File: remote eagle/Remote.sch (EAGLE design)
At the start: 29 parts, among them U1 ATTINY84-20SSU

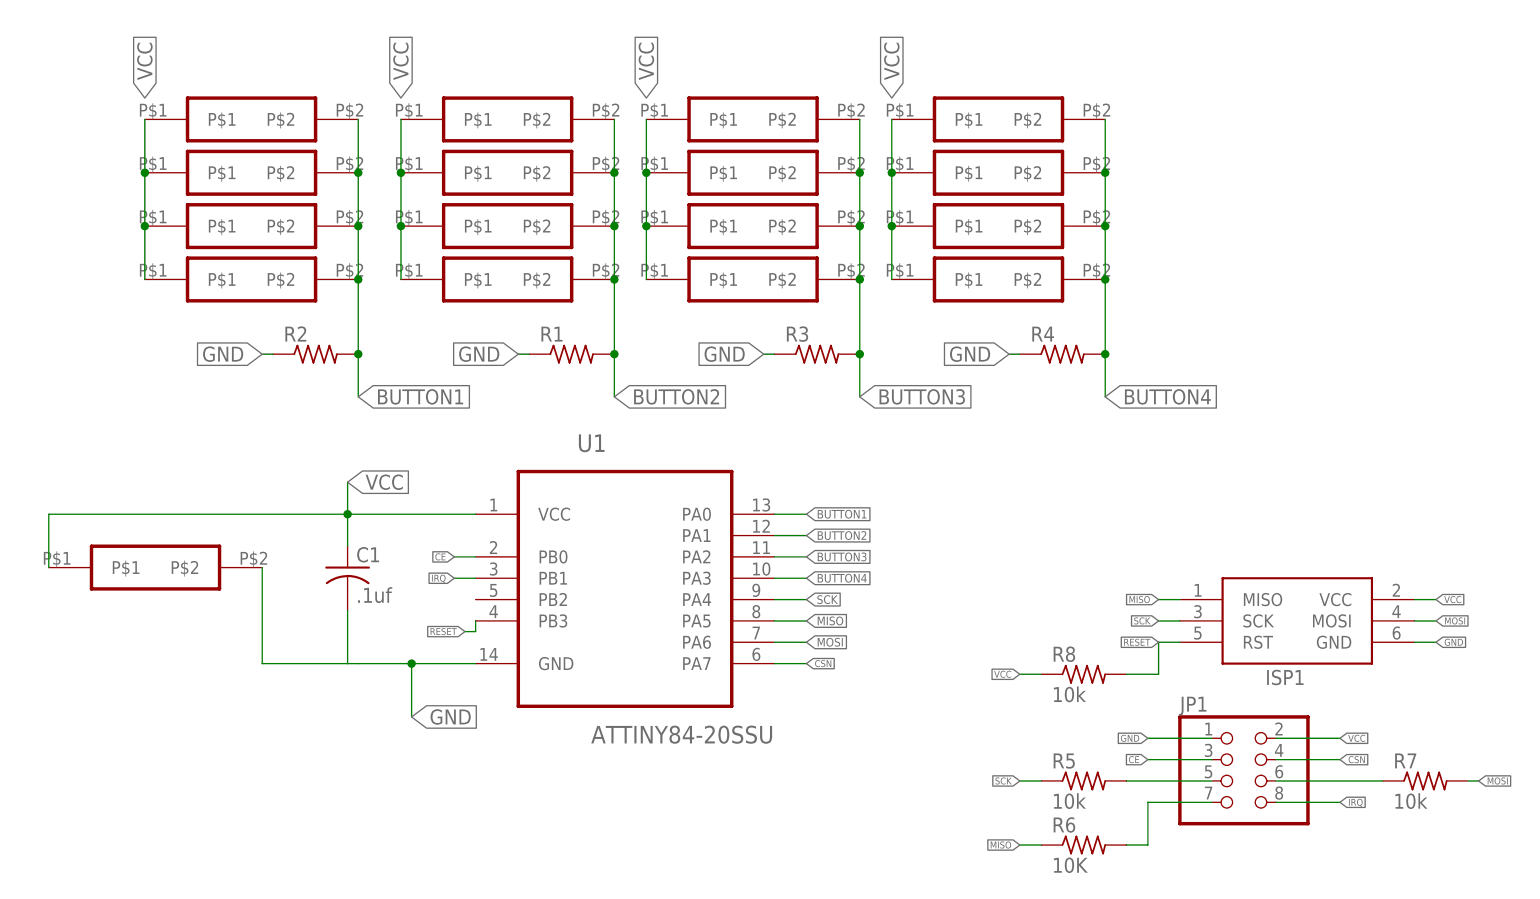
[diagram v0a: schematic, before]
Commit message: Updating remote schematic to include new crystal.
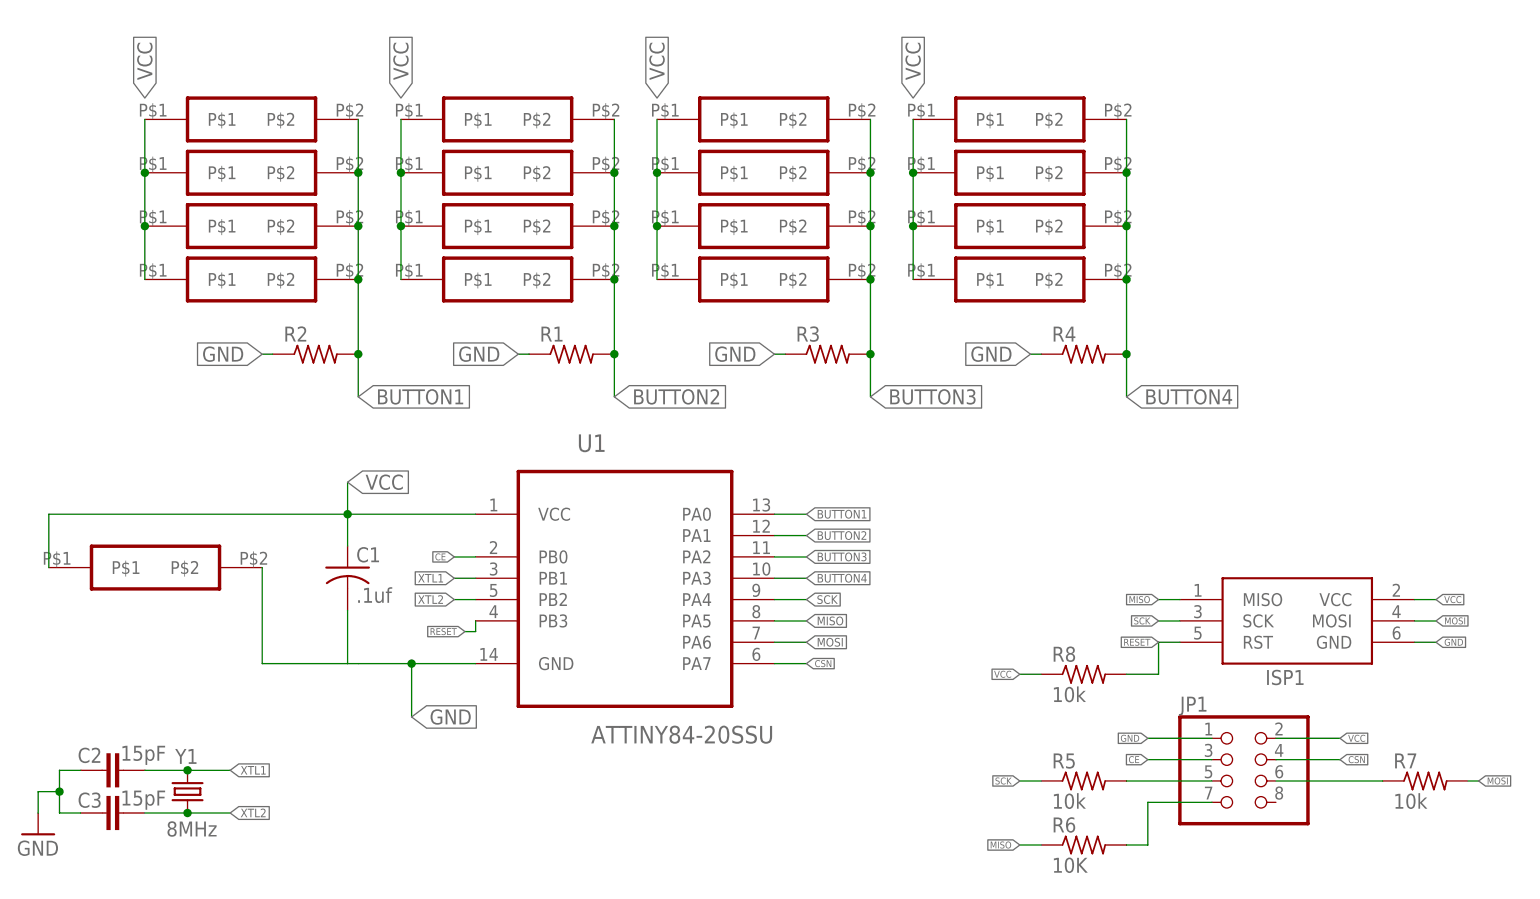
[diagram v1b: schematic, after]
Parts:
- added C2, C3: 15pF, SparkFun:CAP0402-CAP
- added Y1: 8MHz, SparkFun:CRYSTAL5X3
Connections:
- removed net IRQ: JP1.8, U1.PB1
- new net XTL1: C2.2, U1.PB1, Y1.2
- new net XTL2: C3.2, U1.PB2, Y1.1
- net GND: now also C2.1, C3.1
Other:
- moved on the sheet: R3, R4

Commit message: Redrawing remote to fit 1.5" layout. Adding library for new tactile switch with SMD.
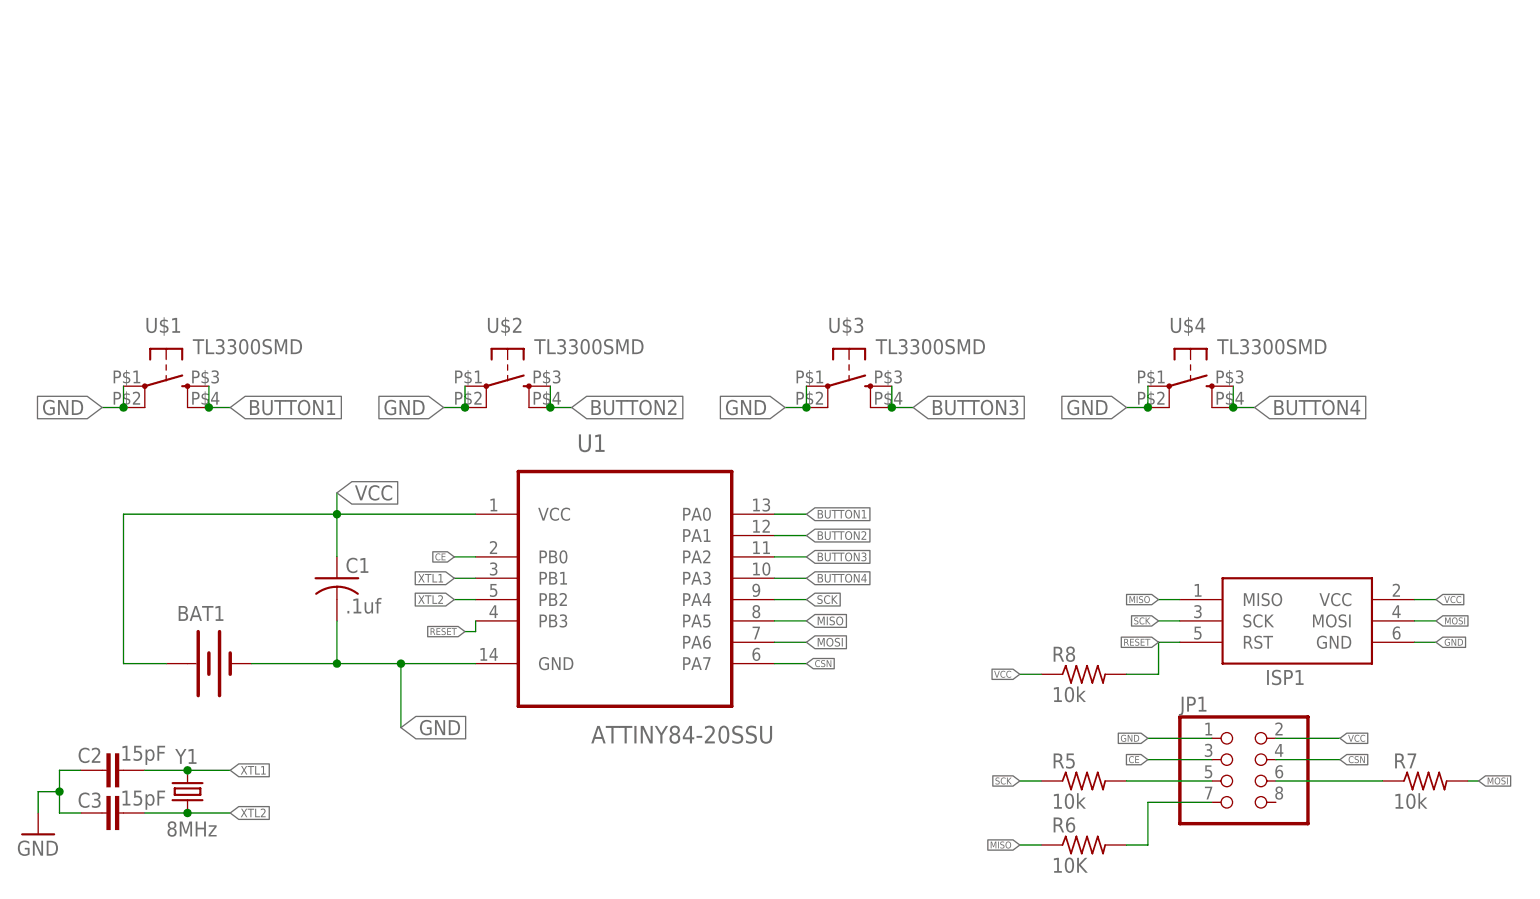
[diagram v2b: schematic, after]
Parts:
- removed BUTTON1-A, BUTTON1-B, BUTTON1-C, BUTTON1-D, BUTTON2-A, BUTTON2-B, BUTTON2-C, BUTTON2-D, BUTTON3-A, BUTTON3-B, BUTTON3-C, BUTTON3-D, BUTTON4-A, BUTTON4-B, BUTTON4-C, BUTTON4-D: BUTTON-25MM-4PAD, solids:BUTTON-25MM-4PAD
- removed R1, R2, R3, R4: (no value), adafruit:R-US_R0805
- added BAT1: (no value), SparkFun-Electromechanical:BATTERY20SMD
- added U$2, U$3, U$4: TL3300SMD, remote:TL3300SMD
- U$1: value A99327CT-ND -> TL3300SMD; device solids:A99327CT-ND -> remote:TL3300SMD
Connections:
- net BUTTON1: now also U$1.S, U$1.S1; no longer BUTTON1-A.P$2, BUTTON1-B.P$2, BUTTON1-C.P$2, BUTTON1-D.P$2, R2.2
- net BUTTON2: now also U$2.S, U$2.S1; no longer BUTTON2-A.P$2, BUTTON2-B.P$2, BUTTON2-C.P$2, BUTTON2-D.P$2, R1.2
- net BUTTON3: now also U$3.S, U$3.S1; no longer BUTTON3-A.P$2, BUTTON3-B.P$2, BUTTON3-C.P$2, BUTTON3-D.P$2, R3.2
- net BUTTON4: now also U$4.S, U$4.S1; no longer BUTTON4-A.P$2, BUTTON4-B.P$2, BUTTON4-C.P$2, BUTTON4-D.P$2, R4.2
- net GND: now also BAT1.-, U$1.P, U$1.P1, U$2.P, U$2.P1, U$3.P, U$3.P1, U$4.P, U$4.P1; no longer R1.1, R2.1, R3.1, R4.1, U$1.P$2
- net VCC: now also BAT1.+; no longer BUTTON1-A.P$1, BUTTON1-B.P$1, BUTTON1-C.P$1, BUTTON1-D.P$1, BUTTON2-A.P$1, BUTTON2-B.P$1, BUTTON2-C.P$1, BUTTON2-D.P$1, BUTTON3-A.P$1, BUTTON3-B.P$1, BUTTON3-C.P$1, BUTTON3-D.P$1, BUTTON4-A.P$1, BUTTON4-B.P$1, BUTTON4-C.P$1, BUTTON4-D.P$1, U$1.P$1
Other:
- moved on the sheet: C1

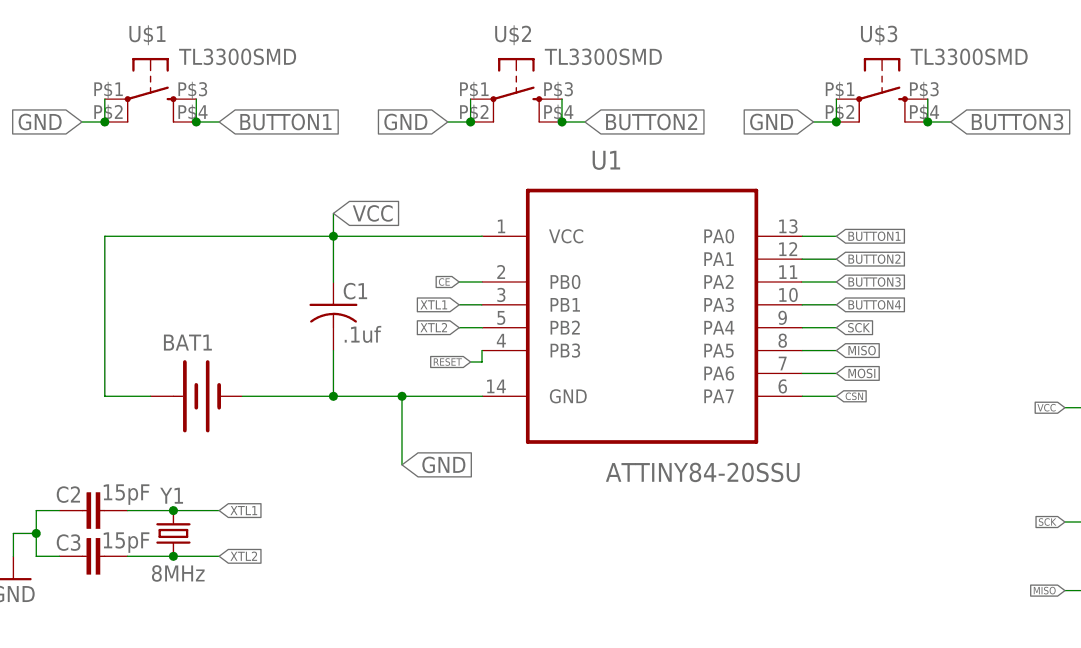
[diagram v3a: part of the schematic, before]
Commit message: Finishing up electrical connections. Replacing battery holder with double-pronged sides.
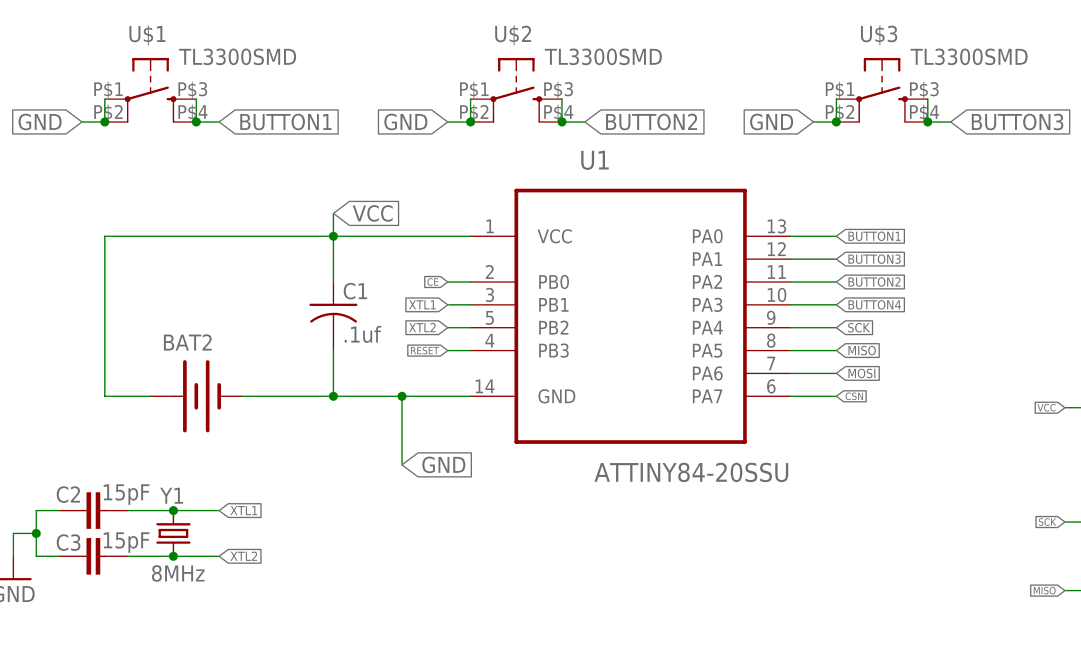
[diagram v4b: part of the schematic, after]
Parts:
- removed BAT1: (no value), SparkFun-Electromechanical:BATTERY20SMD
- added BAT2: (no value), SparkFun-Electromechanical:BATTERY20MM_4LEGS_OVERPASTE
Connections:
- net BUTTON2: now also U1.PA2; no longer U1.PA1
- net BUTTON3: now also U1.PA1; no longer U1.PA2
- net GND: now also BAT2.-; no longer BAT1.-
- net VCC: now also BAT2.+; no longer BAT1.+
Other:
- moved on the sheet: U1

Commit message: Finishing remote rev. 2 board with new buttons and bigger size.
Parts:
- removed C2, C3: 15pF, SparkFun:CAP0402-CAP
- added C5, C6: 15pF, SparkFun-Passives:CAP0805
- U$1, U$2, U$3, U$4: value TL3300SMD -> 5GSH9; device remote:TL3300SMD -> remote:5GSH9
- renumbered ISP1 to ISP, JP1 to NRF24L01, U1 to ATTINY84
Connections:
- net CE: now also ATTINY84.PB2; no longer ATTINY84.PB0
- net GND: now also C5.1, C6.1; no longer C2.1, C3.1
- net XTL1: now also ATTINY84.PB0, C5.2; no longer ATTINY84.PB1, C2.2
- net XTL2: now also ATTINY84.PB1, C6.2; no longer ATTINY84.PB2, C3.2

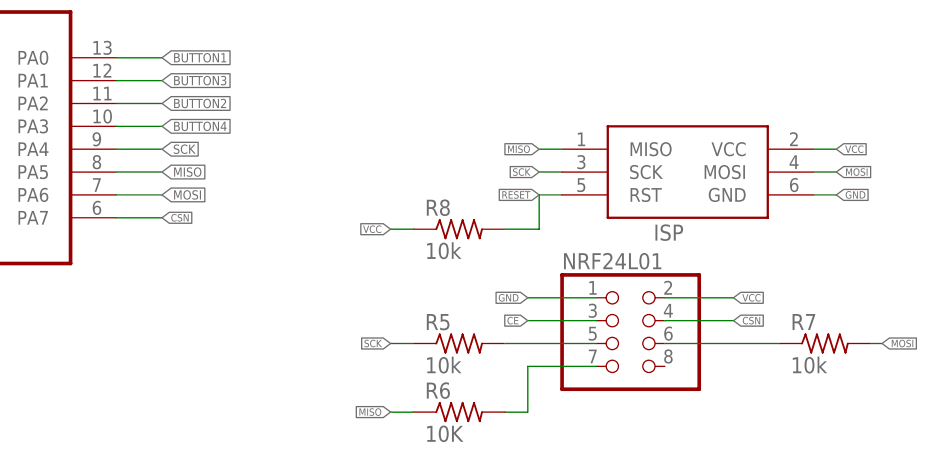
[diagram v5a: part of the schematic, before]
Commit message: Fixing pcb issue by realizing mosi/miso are switched on pcb, and no resistors needed.
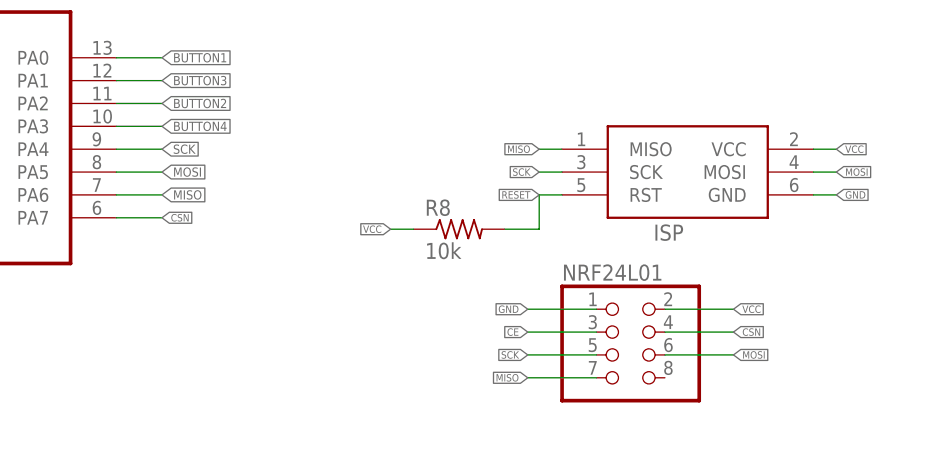
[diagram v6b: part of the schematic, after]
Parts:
- removed R5, R7: 10k, adafruit:R-US_R0805
- removed R6: 10K, adafruit:R-US_R0805
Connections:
- removed net N$2: NRF24L01.5, R5.2
- removed net N$3: NRF24L01.7, R6.2
- removed net N$4: NRF24L01.6, R7.1
- net MISO: now also ATTINY84.PA6, NRF24L01.7; no longer ATTINY84.PA5, R6.1
- net MOSI: now also ATTINY84.PA5, NRF24L01.6; no longer ATTINY84.PA6, R7.2
- net SCK: now also NRF24L01.5; no longer R5.1
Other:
- moved on the sheet: NRF24L01
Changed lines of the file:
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@@
 <part name="ISP" library="adafruit" deviceset="AVRISP" device="-6"/>
 <part name="NRF24L01" library="pinhead" deviceset="PINHD-2X4" device=""/>
-<part name="R5" library="adafruit" deviceset="R-US_" device="R0805" value="10k"/>
-<part name="R6" library="adafruit" deviceset="R-US_" device="R0805" value="10K"/>
-<part name="R7" library="adafruit" deviceset="R-US_" device="R0805" value="10k"/>
 <part name="R8" library="adafruit" deviceset="R-US_" device="R0805" value="10k"/>
 <part name="Y1" library="SparkFun" deviceset="CRYSTAL" device="5X3" value="8MHz"/>
@@
 <instance part="C1" gate="G$1" x="43.18" y="20.32"/>
 <instance part="ISP" gate="G$1" x="156.21" y="15.24"/>
-<instance part="NRF24L01" gate="A" x="149.86" y="-3.81"/>
-<instance part="R5" gate="G$1" x="132.08" y="-3.81"/>
-<instance part="R6" gate="G$1" x="132.08" y="-11.43"/>
-<instance part="R7" gate="G$1" x="172.72" y="-3.81"/>
+<instance part="NRF24L01" gate="A" x="149.86" y="-5.08"/>
 <instance part="R8" gate="G$1" x="132.08" y="8.89"/>
 <instance part="Y1" gate="G$1" x="25.4" y="-5.08" smashed="yes" rot="R90">
@@
 <segment>
 <pinref part="NRF24L01" gate="A" pin="1"/>
-<wire x1="147.32" y1="1.27" x2="139.7" y2="1.27" width="0.1524" layer="91"/>
-<label x="139.7" y="1.27" size="0.8128" layer="95" rot="R180" xref="yes"/>
+<wire x1="147.32" y1="0" x2="139.7" y2="0" width="0.1524" layer="91"/>
+<label x="139.7" y="0" size="0.8128" layer="95" rot="R180" xref="yes"/>
 </segment>
 <segment>
@@
 <net name="MISO" class="0">
 <segment>
-<pinref part="ATTINY84" gate="A" pin="PA5"/>
-<wire x1="93.98" y1="15.24" x2="99.06" y2="15.24" width="0.1524" layer="91"/>
-<label x="99.06" y="15.24" size="1.016" layer="95" xref="yes"/>
-</segment>
-<segment>
 <pinref part="ISP" gate="G$1" pin="MISO"/>
 <wire x1="143.51" y1="17.78" x2="140.97" y2="17.78" width="0.1524" layer="91"/>
@@
 </segment>
 <segment>
-<pinref part="R6" gate="G$1" pin="1"/>
-<wire x1="127" y1="-11.43" x2="124.46" y2="-11.43" width="0.1524" layer="91"/>
-<label x="124.46" y="-11.43" size="0.8128" layer="95" rot="R180" xref="yes"/>
-</segment>
-</net>
-<net name="MOSI" class="0">
+<wire x1="147.32" y1="-7.62" x2="139.7" y2="-7.62" width="0.1524" layer="91"/>
+<label x="139.7" y="-7.62" size="0.8128" layer="95" rot="R180" xref="yes"/>
+<pinref part="NRF24L01" gate="A" pin="7"/>
+</segment>
 <segment>
 <pinref part="ATTINY84" gate="A" pin="PA6"/>
 <wire x1="93.98" y1="12.7" x2="99.06" y2="12.7" width="0.1524" layer="91"/>
-<label x="99.06" y="12.7" size="1.016" layer="95" xref="yes"/>
-</segment>
+<label x="99.06" y="12.7" size="1.016" layer="95" font="vector" xref="yes"/>
+</segment>
+</net>
+<net name="MOSI" class="0">
 <segment>
 <pinref part="ISP" gate="G$1" pin="MOSI"/>
@@
 </segment>
 <segment>
-<pinref part="R7" gate="G$1" pin="2"/>
-<wire x1="177.8" y1="-3.81" x2="179.07" y2="-3.81" width="0.1524" layer="91"/>
-<label x="179.07" y="-3.81" size="0.8128" layer="95" xref="yes"/>
+<wire x1="154.94" y1="-5.08" x2="162.56" y2="-5.08" width="0.1524" layer="91"/>
+<label x="162.56" y="-5.08" size="0.8128" layer="95" xref="yes"/>
+<pinref part="NRF24L01" gate="A" pin="6"/>
+</segment>
+<segment>
+<pinref part="ATTINY84" gate="A" pin="PA5"/>
+<wire x1="93.98" y1="15.24" x2="99.06" y2="15.24" width="0.1524" layer="91"/>
+<label x="99.06" y="15.24" size="1.016" layer="95" font="vector" xref="yes"/>
 </segment>
 </net>
@@
 </segment>
 <segment>
-<pinref part="R5" gate="G$1" pin="1"/>
-<wire x1="127" y1="-3.81" x2="124.46" y2="-3.81" width="0.1524" layer="91"/>
-<label x="124.46" y="-3.81" size="0.8128" layer="95" rot="R180" xref="yes"/>
+<label x="139.7" y="-5.08" size="0.8128" layer="95" rot="R180" xref="yes"/>
+<pinref part="NRF24L01" gate="A" pin="5"/>
+<wire x1="139.7" y1="-5.08" x2="147.32" y2="-5.08" width="0.1524" layer="91"/>
 </segment>
 </net>
@@
 <segment>
 <pinref part="NRF24L01" gate="A" pin="2"/>
-<wire x1="154.94" y1="1.27" x2="162.56" y2="1.27" width="0.1524" layer="91"/>
-<label x="162.56" y="1.27" size="0.8128" layer="95" xref="yes"/>
+<wire x1="154.94" y1="0" x2="162.56" y2="0" width="0.1524" layer="91"/>
+<label x="162.56" y="0" size="0.8128" layer="95" xref="yes"/>
 </segment>
 <segment>
@@
 <segment>
 <pinref part="NRF24L01" gate="A" pin="3"/>
-<wire x1="147.32" y1="-1.27" x2="139.7" y2="-1.27" width="0.1524" layer="91"/>
-<label x="139.7" y="-1.27" size="0.8128" layer="95" rot="R180" xref="yes"/>
+<wire x1="147.32" y1="-2.54" x2="139.7" y2="-2.54" width="0.1524" layer="91"/>
+<label x="139.7" y="-2.54" size="0.8128" layer="95" rot="R180" xref="yes"/>
 </segment>
 <segment>
@@
 <segment>
 <pinref part="NRF24L01" gate="A" pin="4"/>
-<wire x1="154.94" y1="-1.27" x2="162.56" y2="-1.27" width="0.1524" layer="91"/>
-<label x="162.56" y="-1.27" size="0.8128" layer="95" xref="yes"/>
+<wire x1="154.94" y1="-2.54" x2="162.56" y2="-2.54" width="0.1524" layer="91"/>
+<label x="162.56" y="-2.54" size="0.8128" layer="95" xref="yes"/>
 </segment>
 <segment>
@@
 </segment>
 </net>
-<net name="N$2" class="0">
-<segment>
-<pinref part="NRF24L01" gate="A" pin="5"/>
-<pinref part="R5" gate="G$1" pin="2"/>
-<wire x1="147.32" y1="-3.81" x2="137.16" y2="-3.81" width="0.1524" layer="91"/>
-</segment>
-</net>
-<net name="N$3" class="0">
-<segment>
-<pinref part="NRF24L01" gate="A" pin="7"/>
-<wire x1="147.32" y1="-6.35" x2="139.7" y2="-6.35" width="0.1524" layer="91"/>
-<wire x1="139.7" y1="-6.35" x2="139.7" y2="-11.43" width="0.1524" layer="91"/>
-<pinref part="R6" gate="G$1" pin="2"/>
-<wire x1="139.7" y1="-11.43" x2="137.16" y2="-11.43" width="0.1524" layer="91"/>
-</segment>
-</net>
-<net name="N$4" class="0">
-<segment>
-<pinref part="NRF24L01" gate="A" pin="6"/>
-<pinref part="R7" gate="G$1" pin="1"/>
-<wire x1="154.94" y1="-3.81" x2="167.64" y2="-3.81" width="0.1524" layer="91"/>
-</segment>
-</net>
